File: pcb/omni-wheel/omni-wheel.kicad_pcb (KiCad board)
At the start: 2 copper layers, 80 x 86 mm, 39 parts, among them IC1 AP63301WU-7, IC2 AP63301WU-7, J2 Motor2_output, J3 Motor4_output, J4 Motor3_output, J6 Motor1_output, J7 12V Input, U1 SN754410NE, U2 SN754410NE, U3 STM32F030R8Tx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

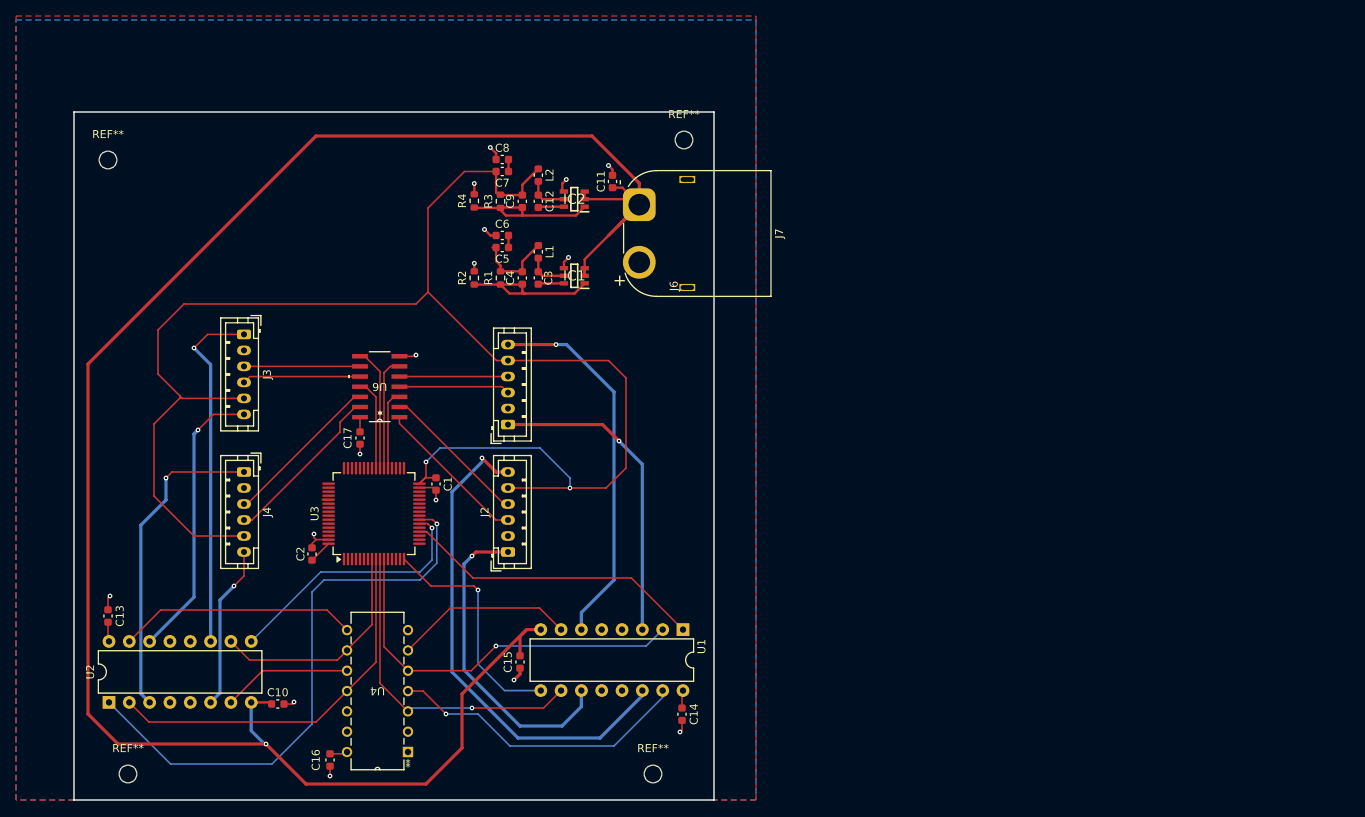
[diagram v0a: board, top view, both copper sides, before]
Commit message: Silkscreen added, just need to add 4-pin jumper, then release!
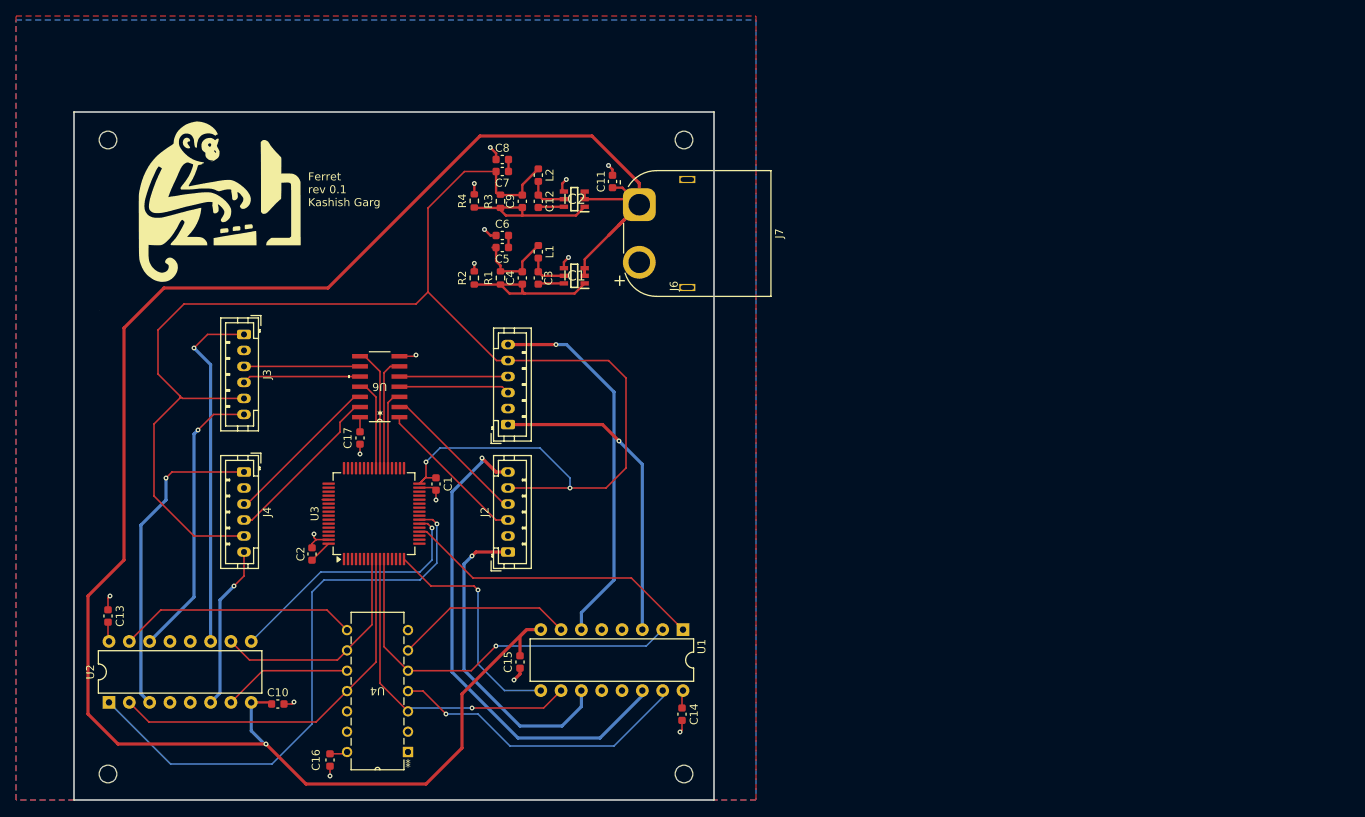
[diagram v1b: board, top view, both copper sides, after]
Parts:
- added G***: LOGO, LOGO, F.Cu at (95.4, 64.7)
- added G***: LOGO, LOGO, B.Cu at (116.5, 69.0)
- moved REF** 3.88 mm to (153.5, 136.8)
- moved REF** 2.50 mm to (81.5, 57.5)
- moved REF** 2.50 mm to (81.5, 136.8)
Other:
- board text added: "Ferret rev 0.1 Kashish Garg"
- board text added: "https://github.com/kashishkebab9/omni-mapper"

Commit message: Added rc uart connections, onto RPI
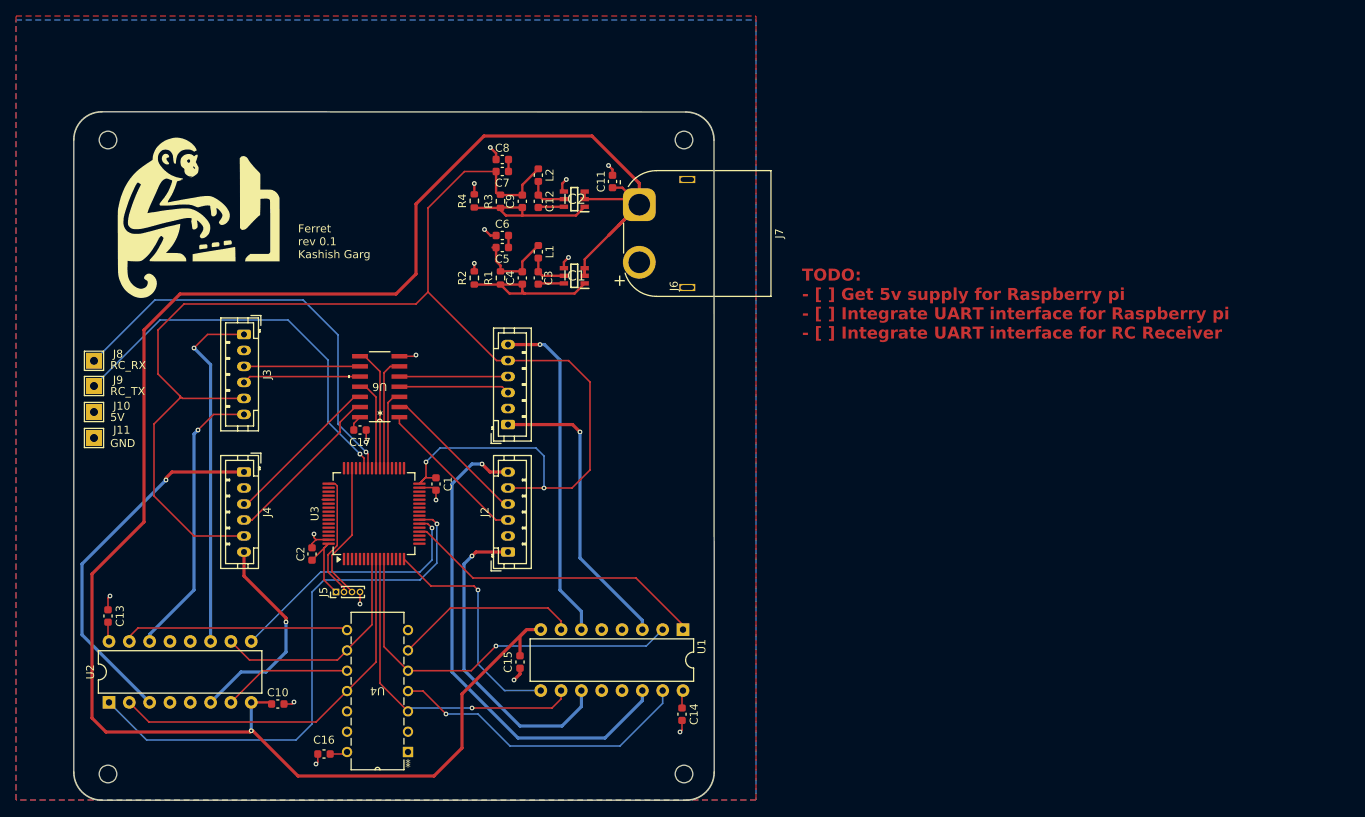
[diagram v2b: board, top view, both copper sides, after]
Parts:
- added J10: Conn_01x01_Pin, TestPoint:TestPoint_THTPad_2.0x2.0mm_Drill1.0mm, F.Cu at (79.8, 91.5)
- added J11: Conn_01x01_Pin, TestPoint:TestPoint_THTPad_2.0x2.0mm_Drill1.0mm, F.Cu at (79.8, 94.8)
- added J5: STLINK, Connector_PinHeader_1.00mm:PinHeader_1x04_P1.00mm_Vertical, F.Cu at (110.0, 114.0)
- added J8: Conn_01x01_Pin, TestPoint:TestPoint_THTPad_2.0x2.0mm_Drill1.0mm, F.Cu at (79.8, 85.1)
- added J9: Conn_01x01_Pin, TestPoint:TestPoint_THTPad_2.0x2.0mm_Drill1.0mm, F.Cu at (79.8, 88.2)
- moved G*** 24.8 mm to (115.2, 93.8)
- moved G*** 3.31 mm to (92.8, 66.8)
- moved C16 1.06 mm to (108.5, 134.2), turned to 180 degrees
- moved C17 1.00 mm to (113.0, 93.8), turned to 0 degrees
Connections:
- U3 pad 42: unconnected-(U3-PA9-Pad42) -> /UART_RC_RX
- U3 pad 43: unconnected-(U3-PA10-Pad43) -> /UART_RC_TX
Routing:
- net /UART_RC_RX: track 0.00 -> 53.7 mm, vias 0 -> 1
- net /UART_RC_TX: track 0.00 -> 50.1 mm, vias 0 -> 1
- net Net-(J5-Pin_3): track 0.00 -> 17.5 mm
- net Net-(J5-Pin_2): track 0.00 -> 15.8 mm
- net +3.3V: track 194.7 -> 183.9 mm
- net Net-(J5-Pin_1): track 2.93 -> 9.84 mm
- net /Motor3_M2: track 20.5 -> 26.7 mm
- net /Motor3_M1: track 39.9 -> 46.0 mm
- net /Motor1_M2: track 47.1 -> 42.1 mm
- net /Motor3_EN: track 71.6 -> 69.1 mm
- net /Motor1_M1: track 39.5 -> 37.3 mm
- net GND: track 28.9 -> 30.8 mm, vias 16 -> 17
- net /Motor4_4A: track 29.9 -> 28.4 mm
- net /Motor1_2A: track 22.4 -> 23.1 mm
- net /Motor2_3A: track 40.7 -> 41.3 mm
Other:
- board size 80 x 86 mm -> 80.1 x 86.1 mm
- board text added: "5V"
- board text added: "GND"
- board text added: "RC_RX"
- board text added: "RC_TX"
- board text added: "TODO: - [ ] Get 5v supply for Raspberry pi - [ ] Integrate UART interface for Raspberry pi - [ ] Integrate UART interface for RC Receiver"

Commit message: Ferret Board rev 0.1 Release
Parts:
- added J15: STLINK, Connector_PinHeader_2.54mm:PinHeader_1x04_P2.54mm_Vertical, F.Cu at (154.4, 93.7)
- J5: footprint Connector_PinHeader_1.00mm:PinHeader_1x04_P1.00mm_Vertical -> Connector_PinHeader_2.54mm:PinHeader_1x04_P2.54mm_Vertical
- moved J11 47.0 mm to (107.7, 57.0), turned to -90 degrees
- moved J8 46.9 mm to (117.3, 57.0), turned to -90 degrees
- moved J10 46.5 mm to (111.0, 57.0), turned to -90 degrees
- moved J9 46.5 mm to (114.2, 57.0), turned to -90 degrees
- moved J5 36.7 mm to (79.8, 93.2), turned to 180 degrees
- moved C2 0.81 mm to (106.2, 109.4)
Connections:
- U3 pad 16: /Motor2_EN -> /UART_RPI_RX
- U3 pad 17: unconnected-(U3-PA3-Pad17) -> /UART_RPI_TX
- U3 pad 35: unconnected-(U3-PB14-Pad35) -> /Motor2_EN
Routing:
- net Net-(J5-Pin_1): track 9.84 -> 65.0 mm, vias 0 -> 1
- net /UART_RPI_RX: track 0.00 -> 53.1 mm, vias 0 -> 1
- net /UART_RPI_TX: track 0.00 -> 52.2 mm, vias 0 -> 1
- net Net-(J5-Pin_3): track 17.5 -> 58.6 mm, vias 0 -> 1
- net Net-(J5-Pin_2): track 15.8 -> 55.6 mm, vias 0 -> 1
- net /Motor2_EN: track 29.3 -> 44.1 mm
- net /UART_RC_RX: track 53.7 -> 51.3 mm
- net /UART_RC_TX: track 50.1 -> 52.2 mm
- net /Motor1_EN: track 38.4 -> 40.4 mm
- net GND: track 30.8 -> 30.0 mm, vias 17 -> 16
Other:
- board text added: "3.3V"
- board text added: "RPI_RX"
- board text added: "RPI_TX"
- board text added: "SWCLK"
- board text added: "SWDIO"
- board text removed: "TODO: - [ ] Get 5v supply for Raspberry pi - [ ] Integrate UART interface for Raspberry pi - [ ] Integrate UART interface for RC Receiver"

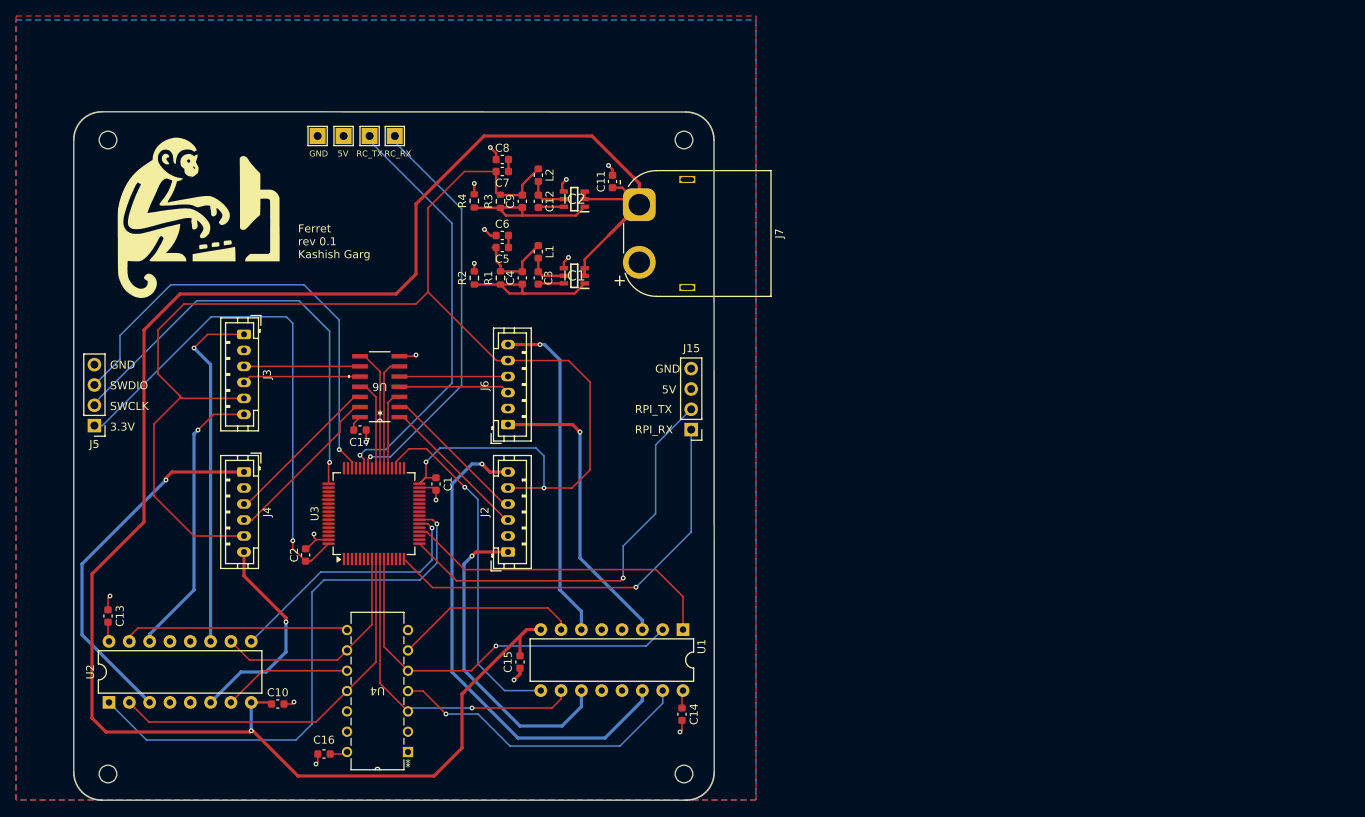
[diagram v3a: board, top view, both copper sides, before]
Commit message: added xt connector step
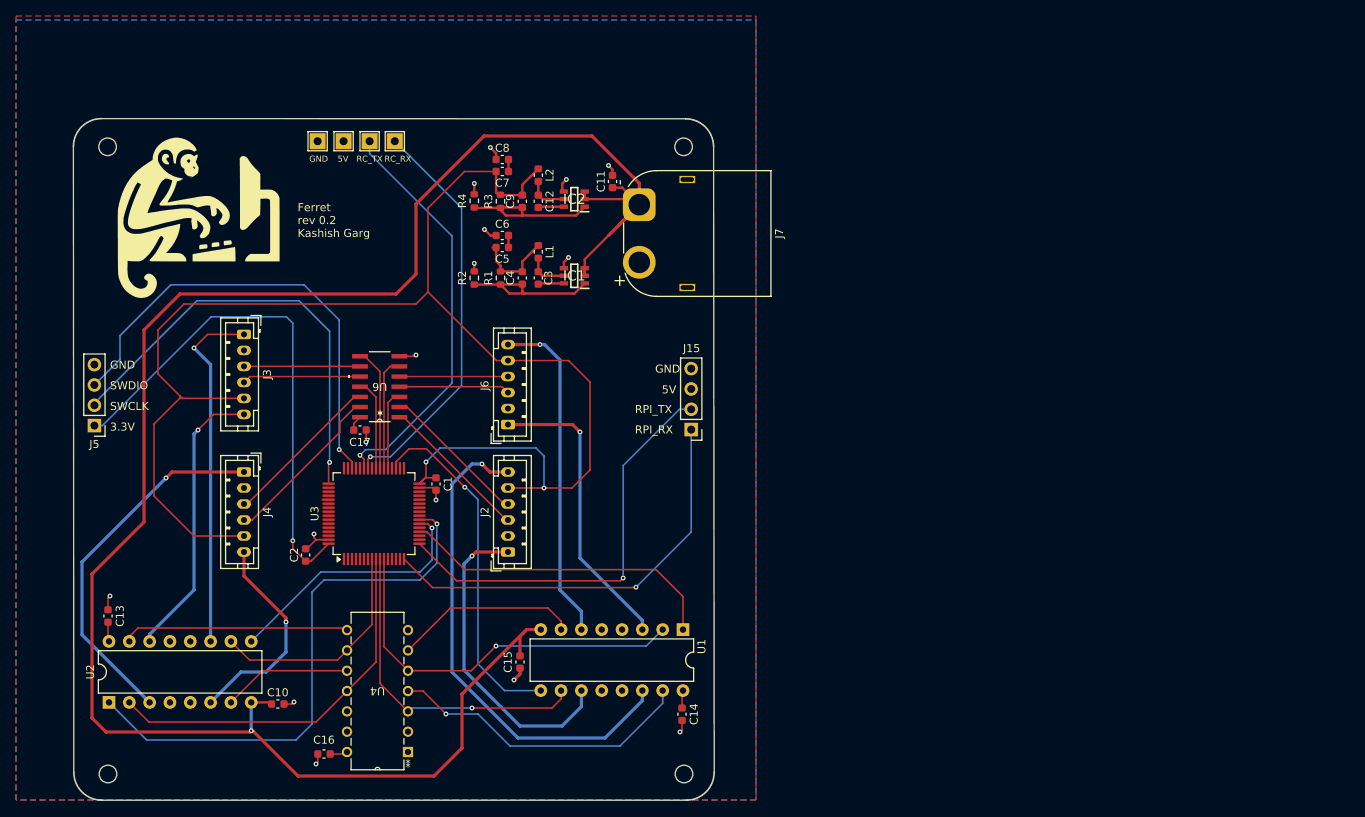
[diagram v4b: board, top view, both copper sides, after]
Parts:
- moved REF** 0.85 mm to (153.4, 58.4)
- moved REF** 0.85 mm to (81.5, 58.4)
- moved J10 0.65 mm to (111.0, 57.6)
- moved J11 0.65 mm to (107.7, 57.6)
- moved J8 0.65 mm to (117.3, 57.6)
- moved J9 0.65 mm to (114.2, 57.6)
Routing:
- net /UART_RPI_TX: track 52.2 -> 53.0 mm
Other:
- board size 80.1 x 86.1 mm -> 80.1 x 85.2 mm
- board text added: "Ferret rev 0.2 Kashish Garg"
- board text removed: "Ferret rev 0.1 Kashish Garg"

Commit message: Added power test points to pcb, going to change xt size and add toggle switch next
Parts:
- removed the G*** at (115.2, 93.8)
- added J1: 12v TP, TestPoint:TestPoint_THTPad_1.0x1.0mm_Drill0.5mm, F.Cu at (79.8, 64.3)
- added J12: 5V TP, TestPoint:TestPoint_THTPad_1.0x1.0mm_Drill0.5mm, F.Cu at (79.8, 67.3)
- added J13: 3.3v TP, TestPoint:TestPoint_THTPad_1.0x1.0mm_Drill0.5mm, F.Cu at (79.8, 70.4)
- added J14: GND TP, TestPoint:TestPoint_THTPad_1.0x1.0mm_Drill0.5mm, F.Cu at (79.8, 73.5)
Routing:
- net +12V: track 249.2 -> 285.8 mm
- net +3.3V: track 183.9 -> 201.2 mm, vias 2 -> 4

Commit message: Added smaller xt connector and power switch
forgot to save schema
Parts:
- added SW1: SW_SPST, GF-123-0054:SW_GF-123-0054, F.Cu at (151.4, 69.5)
- J7: footprint Connector_AMASS:AMASS_XT60PW-M_1x02_P7.20mm_Horizontal -> Connector_AMASS:AMASS_XT30PW-M_1x02_P2.50mm_Horizontal
- moved J7 23.3 mm to (145.4, 88.8)
- moved J15 12.8 mm to (154.2, 106.5)
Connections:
- J7 pad 1: +12V -> Net-(J7-Pin_1)
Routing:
- net Net-(J7-Pin_1): track 0.00 -> 16.7 mm
- net /UART_RPI_TX: track 53.0 -> 39.2 mm
- net /UART_RPI_RX: track 53.1 -> 40.3 mm
- net +12V: track 285.8 -> 288.5 mm
